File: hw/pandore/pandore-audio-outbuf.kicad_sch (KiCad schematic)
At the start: 19 parts, among them U15 OPAMP_DIFF_1

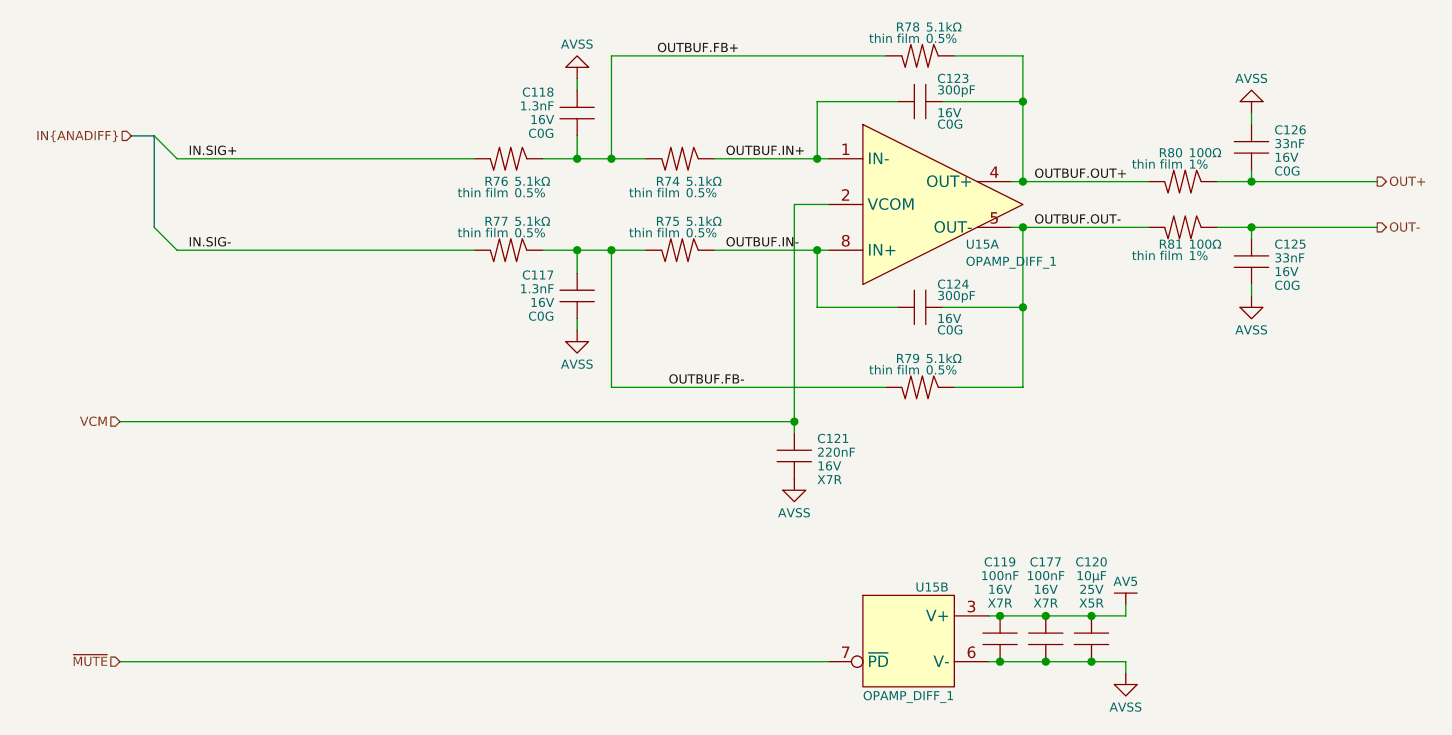
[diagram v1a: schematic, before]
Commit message: finished adding mpn,mfg to all parts, finished routing placement
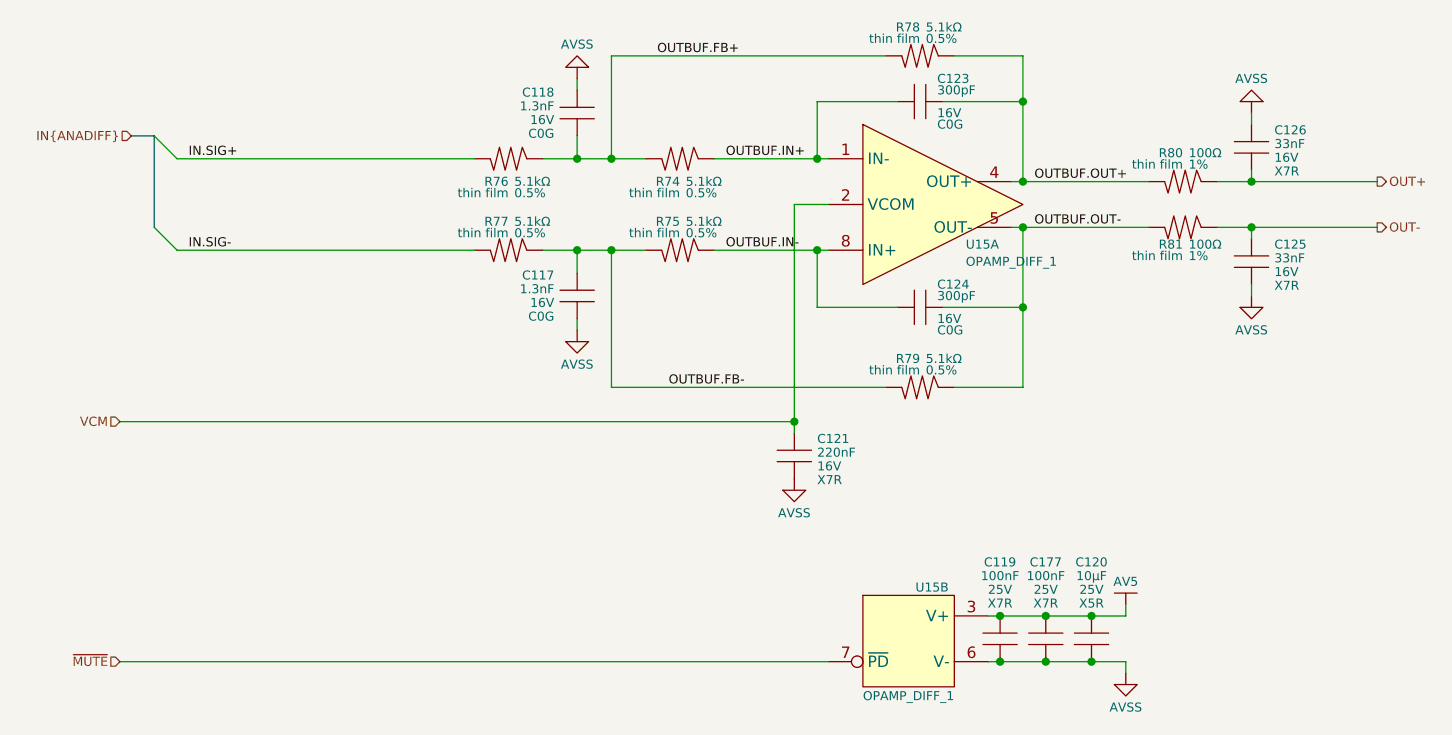
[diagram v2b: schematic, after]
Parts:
- C117, C118: MFG (none) -> Murata; MPN (none) -> GRM1885C1H132JA01D
- C119, C177: MFG2 Samsung Electro-Mechanics -> (none); MFG3 Taiyo Yuden -> (none); MPN2 CL05B104KA5NNNC -> (none); MPN3 EMK105B7104KV-F -> (none); Voltage 16V -> 25V
- C120: MFG (none) -> Murata; MPN (none) -> GRM21BR61E106KA73K
- C121: MFG (none) -> Murata; MPN (none) -> GRM155R71C224KA12D
- C123, C124: MFG (none) -> Walsin Technology Corporation; MPN (none) -> 0603N301J500CT
- C125, C126: Dielectric C0G -> X7R; MFG (none) -> Samsung Electro-Mechanics; MPN (none) -> CL10B333KB8WPNC
- R74, R75, R76, R77, R78, R79: Link (none) -> https://yageogroup.com/products/Resistors/part/RT0805DRE075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
- R80, R81: MFG (none) -> Susumu; MPN (none) -> RR1220P-101-D; Power 0.25W -> 250mW
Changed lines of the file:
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@@
 			)
 		)
-		(property "Datasheet" ""
+		(property "Datasheet" "https://search.murata.co.jp/Ceramy/image/img/A01X/G101/ENG/GRM21BR61E106KA73-01.pdf"
 			(at 157.48 138.938 0)
 			(do_not_autoplace yes)
@@
 			)
 		)
-		(property "MPN" ""
+		(property "MPN" "GRM21BR61E106KA73K"
 			(at 157.48 143.256 0)
 			(do_not_autoplace yes)
@@
 			)
 		)
-		(property "MFG" ""
+		(property "MFG" "Murata"
 			(at 169.418 143.256 0)
 			(do_not_autoplace yes)
@@
 			)
 		)
-		(property "Voltage" "16V"
+		(property "Voltage" "25V"
 			(at 152.4 118.999 0)
 			(do_not_autoplace yes)
@@
 			)
 		)
-		(property "MPN2" "CL05B104KA5NNNC"
+		(property "MPN2" ""
 			(at 152.4 144.78 0)
 			(do_not_autoplace yes)
@@
 			)
 		)
-		(property "MFG2" "Samsung Electro-Mechanics"
+		(property "MFG2" ""
 			(at 164.338 144.78 0)
 			(do_not_autoplace yes)
@@
 			)
 		)
-		(property "MPN3" "EMK105B7104KV-F"
+		(property "MPN3" ""
 			(at 152.4 146.304 0)
 			(do_not_autoplace yes)
@@
 			)
 		)
-		(property "MFG3" "Taiyo Yuden"
+		(property "MFG3" ""
 			(at 164.338 146.304 0)
 			(do_not_autoplace yes)
@@
 			)
 		)
-		(property "Datasheet" ""
+		(property "Datasheet" "https://www.susumu.co.jp/common/pdf/n_catalog_partition05_en.pdf"
 			(at 181.864 73.66 0)
 			(do_not_autoplace yes)
@@
 			)
 		)
-		(property "Power" "0.25W"
+		(property "Power" "250mW"
 			(at 167.64 71.755 90)
 			(do_not_autoplace yes)
@@
 			)
 		)
-		(property "MPN" ""
+		(property "MPN" "RR1220P-101-D"
 			(at 185.42 73.66 0)
 			(do_not_autoplace yes)
@@
 			)
 		)
-		(property "MFG" ""
+		(property "MFG" "Susumu"
 			(at 185.166 59.69 0)
 			(do_not_autoplace yes)
@@
 			)
 		)
-		(property "Datasheet" ""
+		(property "Datasheet" "https://www.passivecomponent.com/wp-content/uploads/datasheet/WTC_MLCC_General_Purpose.pdf"
 			(at 152.908 87.63 0)
 			(do_not_autoplace yes)
@@
 			)
 		)
-		(property "MPN" ""
+		(property "MPN" "0603N301J500CT"
 			(at 157.226 87.63 0)
 			(do_not_autoplace yes)
@@
 			)
 		)
-		(property "MFG" ""
+		(property "MFG" "Walsin Technology Corporation"
 			(at 157.226 99.568 0)
 			(do_not_autoplace yes)
@@
 			)
 		)
-		(property "Datasheet" ""
+		(property "Datasheet" "https://www.passivecomponent.com/wp-content/uploads/datasheet/WTC_MLCC_General_Purpose.pdf"
 			(at 152.908 64.77 0)
 			(do_not_autoplace yes)
@@
 			)
 		)
-		(property "MPN" ""
+		(property "MPN" "0603N301J500CT"
 			(at 157.226 64.77 0)
 			(do_not_autoplace yes)
@@
 			)
 		)
-		(property "MFG" ""
+		(property "MFG" "Walsin Technology Corporation"
 			(at 157.226 76.708 0)
 			(do_not_autoplace yes)
@@
 			)
 		)
-		(property "Link" ""
+		(property "Link" "https://yageogroup.com/products/Resistors/part/RT0805DRE075K1L"
 			(at 108.458 81.026 0)
 			(do_not_autoplace yes)
@@
 			)
 		)
-		(property "Link" ""
+		(property "Link" "https://yageogroup.com/products/Resistors/part/RT0805DRE075K1L"
 			(at 127.508 81.026 0)
 			(do_not_autoplace yes)
@@
 			)
 		)
-		(property "Link" ""
+		(property "Link" "https://yageogroup.com/products/Resistors/part/RT0805DRE075K1L"
 			(at 154.178 59.436 0)
 			(do_not_autoplace yes)
@@
 			)
 		)
-		(property "Link" ""
+		(property "Link" "https://yageogroup.com/products/Resistors/part/RT0805DRE075K1L"
 			(at 127.508 70.866 0)
 			(do_not_autoplace yes)
@@
 			)
 		)
-		(property "Datasheet" ""
+		(property "Datasheet" "https://search.murata.co.jp/Ceramy/image/img/A01X/G101/ENG/GRM155R71C224KA12-01.pdf"
 			(at 124.46 118.618 0)
 			(do_not_autoplace yes)
@@
 			)
 		)
-		(property "MPN" ""
+		(property "MPN" "GRM155R71C224KA12D"
 			(at 124.46 122.936 0)
 			(do_not_autoplace yes)
@@
 			)
 		)
-		(property "MFG" ""
+		(property "MFG" "Murata"
 			(at 136.398 122.936 0)
 			(do_not_autoplace yes)
@@
 			)
 		)
-		(property "Datasheet" ""
+		(property "Datasheet" "https://mm.digikey.com/Volume0/opasdata/d220001/medias/docus/41/CL10B333KB8WPNC_Spec.pdf"
 			(at 175.26 97.028 0)
 			(do_not_autoplace yes)
@@
 			)
 		)
-		(property "Dielectric" "C0G"
+		(property "Dielectric" "X7R"
 			(at 177.8 85.217 0)
 			(do_not_autoplace yes)
@@
 			)
 		)
-		(property "MPN" ""
+		(property "MPN" "CL10B333KB8WPNC"
 			(at 175.26 101.346 0)
 			(do_not_autoplace yes)
@@
 			)
 		)
-		(property "MFG" ""
+		(property "MFG" "Samsung Electro-Mechanics"
 			(at 163.322 101.346 0)
 			(do_not_autoplace yes)
@@
 			)
 		)
-		(property "Link" ""
+		(property "Link" "https://yageogroup.com/products/Resistors/part/RT0805DRE075K1L"
 			(at 108.458 70.866 0)
 			(do_not_autoplace yes)
@@
 			)
 		)
-		(property "Datasheet" ""
+		(property "Datasheet" "https://search.murata.co.jp/Ceramy/image/img/A01X/G101/ENG/GRM1885C1H132JA01-01A.pdf"
 			(at 100.33 80.518 0)
 			(do_not_autoplace yes)
@@
 			)
 		)
-		(property "MPN" ""
+		(property "MPN" "GRM1885C1H132JA01D"
 			(at 100.33 84.836 0)
 			(do_not_autoplace yes)
@@
 			)
 		)
-		(property "MFG" ""
+		(property "MFG" "Murata"
 			(at 88.392 84.836 0)
 			(do_not_autoplace yes)
@@
 			)
 		)
-		(property "Link" ""
+		(property "Link" "https://yageogroup.com/products/Resistors/part/RT0805DRE075K1L"
 			(at 154.178 96.266 0)
 			(do_not_autoplace yes)
@@
 			)
 		)
-		(property "Datasheet" ""
+		(property "Datasheet" "https://search.murata.co.jp/Ceramy/image/img/A01X/G101/ENG/GRM1885C1H132JA01-01A.pdf"
 			(at 100.33 100.838 0)
 			(do_not_autoplace yes)
@@
 			)
 		)
-		(property "MPN" ""
+		(property "MPN" "GRM1885C1H132JA01D"
 			(at 100.33 105.156 0)
 			(do_not_autoplace yes)
@@
 			)
 		)
-		(property "MFG" ""
+		(property "MFG" "Murata"
 			(at 88.392 105.156 0)
 			(do_not_autoplace yes)
@@
 			)
 		)
-		(property "Datasheet" ""
+		(property "Datasheet" "https://mm.digikey.com/Volume0/opasdata/d220001/medias/docus/41/CL10B333KB8WPNC_Spec.pdf"
 			(at 175.26 84.328 0)
 			(do_not_autoplace yes)
@@
 			)
 		)
-		(property "Dielectric" "C0G"
+		(property "Dielectric" "X7R"
 			(at 177.8 72.517 0)
 			(do_not_autoplace yes)
@@
 			)
 		)
-		(property "MPN" ""
+		(property "MPN" "CL10B333KB8WPNC"
 			(at 175.26 88.646 0)
 			(do_not_autoplace yes)
@@
 			)
 		)
-		(property "MFG" ""
+		(property "MFG" "Samsung Electro-Mechanics"
 			(at 163.322 88.646 0)
 			(do_not_autoplace yes)
@@
 			)
 		)
-		(property "Datasheet" ""
+		(property "Datasheet" "https://www.susumu.co.jp/common/pdf/n_catalog_partition05_en.pdf"
 			(at 181.864 78.74 0)
 			(do_not_autoplace yes)
@@
 			)
 		)
-		(property "Power" "0.25W"
+		(property "Power" "250mW"
 			(at 167.64 76.835 90)
 			(do_not_autoplace yes)
@@
 			)
 		)
-		(property "MPN" ""
+		(property "MPN" "RR1220P-101-D"
 			(at 185.42 78.74 0)
 			(do_not_autoplace yes)
@@
 			)
 		)
-		(property "MFG" ""
+		(property "MFG" "Susumu"
 			(at 185.166 64.77 0)
 			(do_not_autoplace yes)
@@
 			)
 		)
-		(property "Voltage" "16V"
+		(property "Voltage" "25V"
 			(at 147.32 118.999 0)
 			(do_not_autoplace yes)
@@
 			)
 		)
-		(property "MPN2" "CL05B104KA5NNNC"
+		(property "MPN2" ""
 			(at 147.32 144.78 0)
 			(do_not_autoplace yes)
@@
 			)
 		)
-		(property "MFG2" "Samsung Electro-Mechanics"
+		(property "MFG2" ""
 			(at 159.258 144.78 0)
 			(do_not_autoplace yes)
@@
 			)
 		)
-		(property "MPN3" "EMK105B7104KV-F"
+		(property "MPN3" ""
 			(at 147.32 146.304 0)
 			(do_not_autoplace yes)
@@
 			)
 		)
-		(property "MFG3" "Taiyo Yuden"
+		(property "MFG3" ""
 			(at 159.258 146.304 0)
 			(do_not_autoplace yes)
